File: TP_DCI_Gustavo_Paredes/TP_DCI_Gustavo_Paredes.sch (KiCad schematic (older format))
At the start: 6 parts, among them X701DB9F/90 DB9_Female, X702DB9M/90 DB9_Male

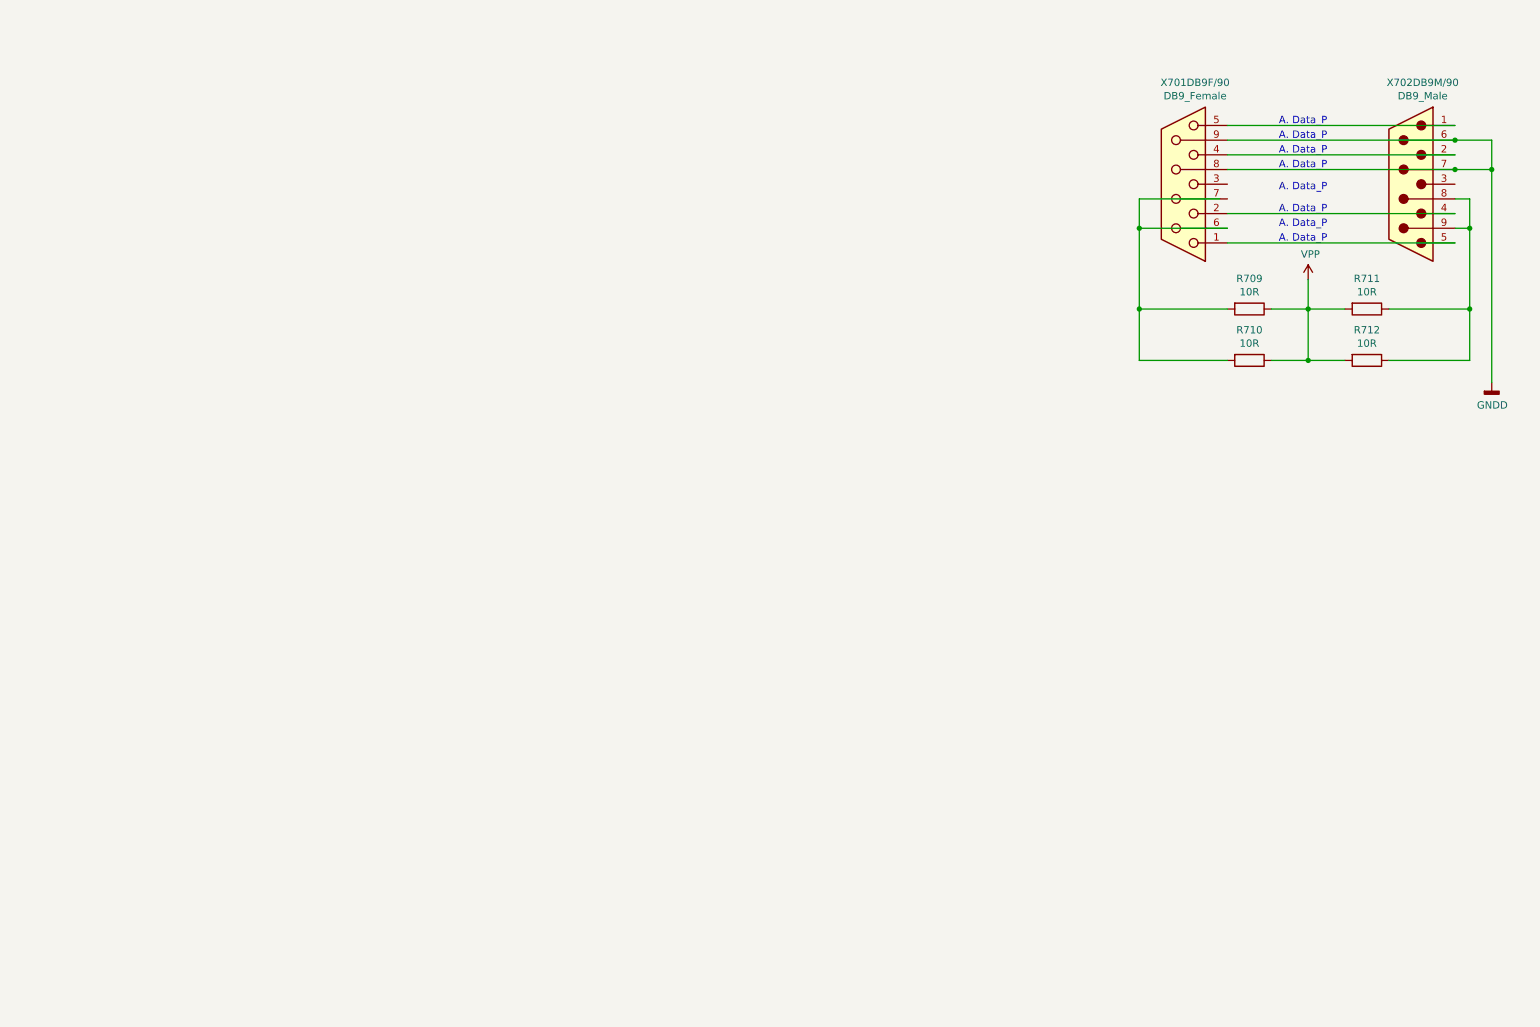
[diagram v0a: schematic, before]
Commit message: Conecciones externas DB9
Se conectaron las conexiones externas del DB9.
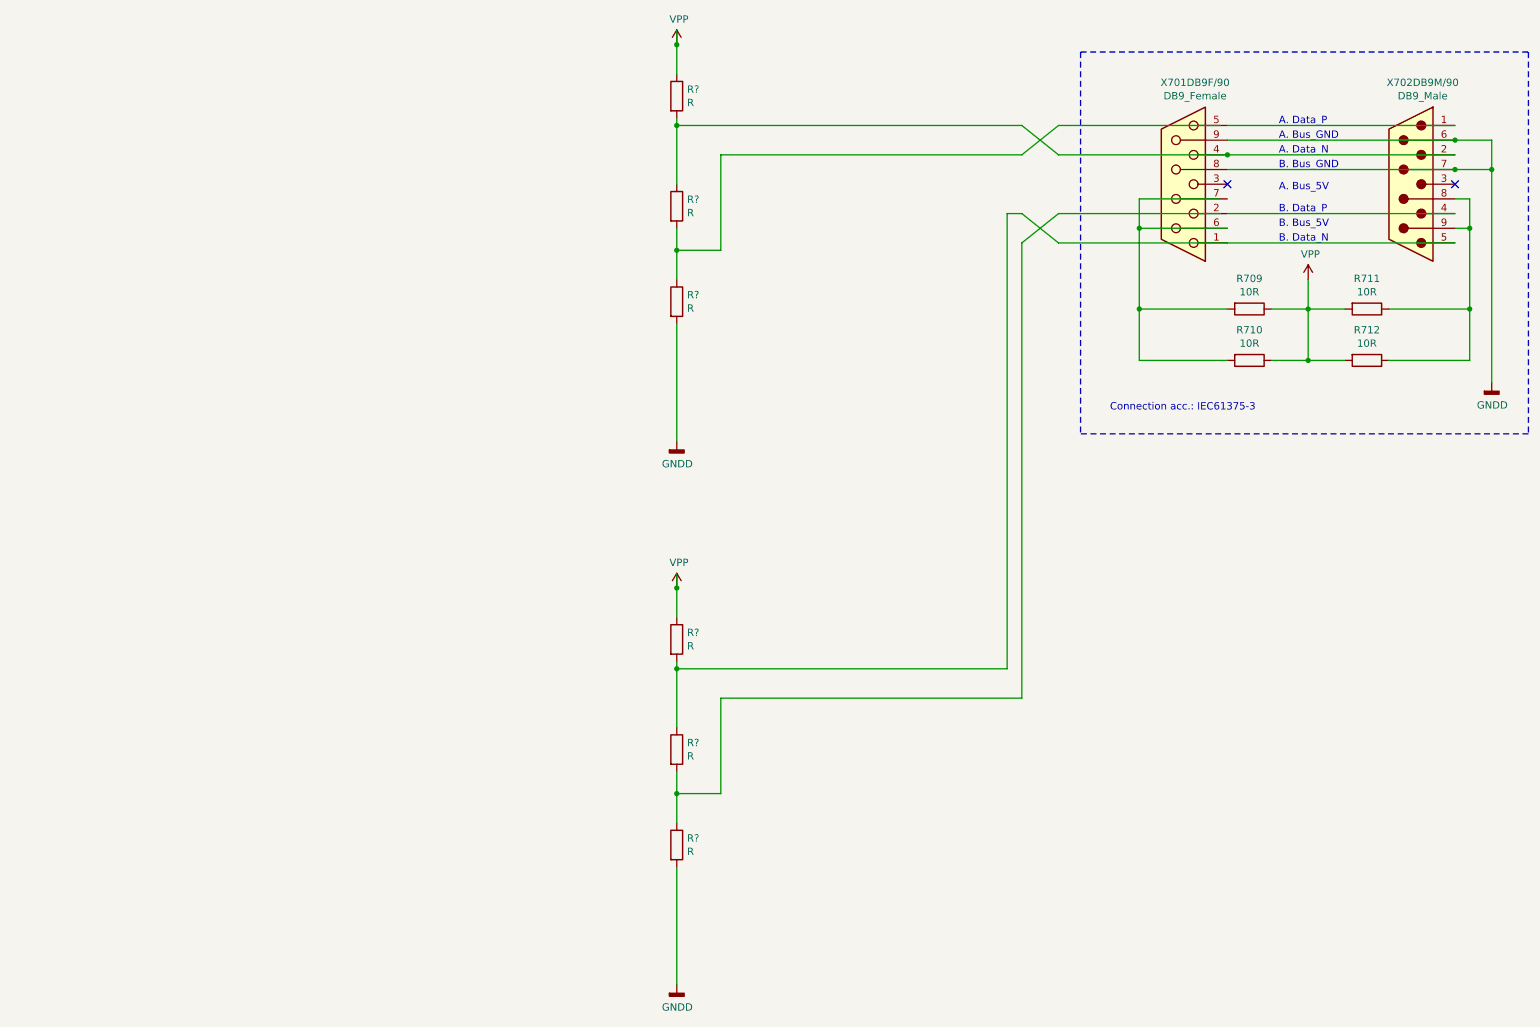
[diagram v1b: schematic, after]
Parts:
- added R? (x6): R, symbol Device:R
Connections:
- wire segments 30 -> 63
- no-connect marks 0 -> 2
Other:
- note added: "A. Bus_5V"
- note added: "A. Bus_GND"
- note added: "A. Data_N"
- note added: "B. Bus_5V"
- note added: "B. Bus_GND"
- note added: "B. Data_N"
- note added: "B. Data_P"
- note added: "Connection acc.: IEC61375-3"
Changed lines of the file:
@@
 A. Data_P
 Text Notes 9250 1500 0    50   ~ 0
-A. Data_P
+A. Bus_GND
 Text Notes 9250 1600 0    50   ~ 0
-A. Data_P
+A. Data_N
 Text Notes 9250 1700 0    50   ~ 0
-A. Data_P
+B. Bus_GND
 Text Notes 9250 1850 0    50   ~ 0
-A. Data_P
+A. Bus_5V
 Text Notes 9250 2000 0    50   ~ 0
-A. Data_P
+B. Data_P
 Text Notes 9250 2100 0    50   ~ 0
-A. Data_P
+B. Bus_5V
 Text Notes 9250 2200 0    50   ~ 0
-A. Data_P
+B. Data_N
+NoConn ~ 10450 1800
+NoConn ~ 8900 1800
+Wire Notes Line width 20 style solid
+	7900 900  10950 900
+Wire Notes Line width 20 style solid
+	10950 900  10950 3500
+Wire Notes Line width 20 style solid
+	10950 3500 7900 3500
+Text Notes 8100 3350 0    50   ~ 0
+Connection acc.: IEC61375-3
+$Comp
+L Device:R R?
+U 1 1 5CE42F3F
+P 5150 1200
+F 0 "R?" H 5220 1246 50  0000 L CNN
+F 1 "R" H 5220 1155 50  0000 L CNN
+F 2 "" V 5080 1200 50  0001 C CNN
+F 3 "~" H 5150 1200 50  0001 C CNN
+	1    5150 1200
+	1    0    0    -1
+$EndComp
+$Comp
+L Device:R R?
+U 1 1 5CE430BC
+P 5150 1950
+F 0 "R?" H 5220 1996 50  0000 L CNN
+F 1 "R" H 5220 1905 50  0000 L CNN
+F 2 "" V 5080 1950 50  0001 C CNN
+F 3 "~" H 5150 1950 50  0001 C CNN
+	1    5150 1950
+	1    0    0    -1
+$EndComp
+$Comp
+L Device:R R?
+U 1 1 5CE430FA
+P 5150 2600
+F 0 "R?" H 5220 2646 50  0000 L CNN
+F 1 "R" H 5220 2555 50  0000 L CNN
+F 2 "" V 5080 2600 50  0001 C CNN
+F 3 "~" H 5150 2600 50  0001 C CNN
+	1    5150 2600
+	1    0    0    -1
+$EndComp
+$Comp
+L power:GNDD #PWR?
+U 1 1 5CE43170
+P 5150 3550
+F 0 "#PWR?" H 5150 3300 50  0001 C CNN
+F 1 "GNDD" H 5154 3395 50  0000 C CNN
+F 2 "" H 5150 3550 50  0001 C CNN
+F 3 "" H 5150 3550 50  0001 C CNN
+	1    5150 3550
+	1    0    0    -1
+$EndComp
+$Comp
+L power:VPP #PWR?
+U 1 1 5CE4319F
+P 5150 850
+F 0 "#PWR?" H 5150 700 50  0001 C CNN
+F 1 "VPP" H 5165 1023 50  0000 C CNN
+F 2 "" H 5150 850 50  0001 C CNN
+F 3 "" H 5150 850 50  0001 C CNN
+	1    5150 850
+	1    0    0    -1
+$EndComp
+Wire Wire Line
+	5150 2100 5150 2250
+Wire Wire Line
+	5150 2750 5150 3550
+Wire Wire Line
+	5150 750  5150 850
+Wire Wire Line
+	8850 1400 7750 1400
+Wire Wire Line
+	8900 1600 7750 1600
+Connection ~ 8900 1600
+Wire Wire Line
+	5150 850  5150 1050
+Connection ~ 5150 850
+Wire Wire Line
+	5150 1800 5150 1400
+Wire Wire Line
+	7500 1400 5150 1400
+Connection ~ 5150 1400
+Wire Wire Line
+	5150 1400 5150 1350
+Wire Wire Line
+	7500 1600 5450 1600
+Wire Wire Line
+	5450 1600 5450 2250
+Wire Wire Line
+	5450 2250 5150 2250
+Connection ~ 5150 2250
+Wire Wire Line
+	5150 2250 5150 2450
+Wire Wire Line
+	7750 1600 7500 1400
+Wire Wire Line
+	7750 1400 7500 1600
+$Comp
+L Device:R R?
+U 1 1 5CE4D6F2
+P 5150 4900
+F 0 "R?" H 5220 4946 50  0000 L CNN
+F 1 "R" H 5220 4855 50  0000 L CNN
+F 2 "" V 5080 4900 50  0001 C CNN
+F 3 "~" H 5150 4900 50  0001 C CNN
+	1    5150 4900
+	1    0    0    -1
+$EndComp
+$Comp
+L Device:R R?
+U 1 1 5CE4D6F9
+P 5150 5650
+F 0 "R?" H 5220 5696 50  0000 L CNN
+F 1 "R" H 5220 5605 50  0000 L CNN
+F 2 "" V 5080 5650 50  0001 C CNN
+F 3 "~" H 5150 5650 50  0001 C CNN
+	1    5150 5650
+	1    0    0    -1
+$EndComp
+$Comp
+L Device:R R?
+U 1 1 5CE4D700
+P 5150 6300
+F 0 "R?" H 5220 6346 50  0000 L CNN
+F 1 "R" H 5220 6255 50  0000 L CNN
+F 2 "" V 5080 6300 50  0001 C CNN
+F 3 "~" H 5150 6300 50  0001 C CNN
+	1    5150 6300
+	1    0    0    -1
+$EndComp
+$Comp
+L power:GNDD #PWR?
+U 1 1 5CE4D707
+P 5150 7250
+F 0 "#PWR?" H 5150 7000 50  0001 C CNN
+F 1 "GNDD" H 5154 7095 50  0000 C CNN
+F 2 "" H 5150 7250 50  0001 C CNN
+F 3 "" H 5150 7250 50  0001 C CNN
+	1    5150 7250
+	1    0    0    -1
+$EndComp
+$Comp
+L power:VPP #PWR?
+U 1 1 5CE4D70D
+P 5150 4550
+F 0 "#PWR?" H 5150 4400 50  0001 C CNN
+F 1 "VPP" H 5165 4723 50  0000 C CNN
+F 2 "" H 5150 4550 50  0001 C CNN
+F 3 "" H 5150 4550 50  0001 C CNN
+	1    5150 4550
+	1    0    0    -1
+$EndComp
+Wire Wire Line
+	5150 5800 5150 5950
+Wire Wire Line
+	5150 6450 5150 7250
+Wire Wire Line
+	5150 4450 5150 4550
+Wire Wire Line
+	5150 4550 5150 4750
+Connection ~ 5150 4550
+Wire Wire Line
+	5450 5300 5450 5950
+Wire Wire Line
+	5450 5950 5150 5950
+Connection ~ 5150 5950
+Wire Wire Line
+	5150 5950 5150 6150
+Wire Wire Line
+	8850 2000 7750 2000
+Wire Wire Line
+	8900 2200 7750 2200
+Wire Wire Line
+	7750 2200 7500 2000
+Wire Wire Line
+	7750 2000 7500 2200
+Wire Wire Line
+	5150 5050 5150 5100
+Wire Wire Line
+	7500 2200 7500 5300
+Wire Wire Line
+	7500 5300 5450 5300
+Wire Wire Line
+	7500 2000 7400 2000
+Wire Wire Line
+	7400 2000 7400 5100
+Wire Wire Line
+	7400 5100 5150 5100
+Connection ~ 5150 5100
+Wire Wire Line
+	5150 5100 5150 5500
+Wire Notes Line width 20 style solid
+	7900 900  7900 3500
 $EndSCHEMATC

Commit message: Saco Ejercicios Practica Clases
Saco a un carpeta externa los ejercicios de las clases.
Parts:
- added C101, C102: 22nF, symbol Device:C
- added D101, D105: 4,7V, symbol Device:D_Zener
- added D102, D104, D106, D108: BAV99, symbol Diode:BAV99
- added D103, D107: 8,2V, symbol Device:D_Zener
- added R101, R102: 10K, symbol Device:R
- added U101, U102: LTC2861, Package_SO:SSOP-28_5.3x10.2mm_P0.65mm, symbol Interface_UART:LTC2861
- R103, R105, R106, R108: renamed from R?; value R -> 68K
- R104, R107: renamed from R?; value R -> 27K
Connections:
- net labels added: LINE_A_D0, LINE_A_D1, LINE_A_SF, LINE_B_D0, LINE_B_D1, LINE_B_SF, P701
- wire segments 63 -> 140
- no-connect marks 2 -> 6
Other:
- note added: "BZX84C4V7"
- note added: "BZX84C8V2"
- note added: "RS485: LINE_A_SF, LINE_A_D0, LINE_A_D1\n LINE_B_SF, LINE_B_D0, LINE_B_D1"
- moved on the sheet: R103, R104, R105, R106, R107, R108

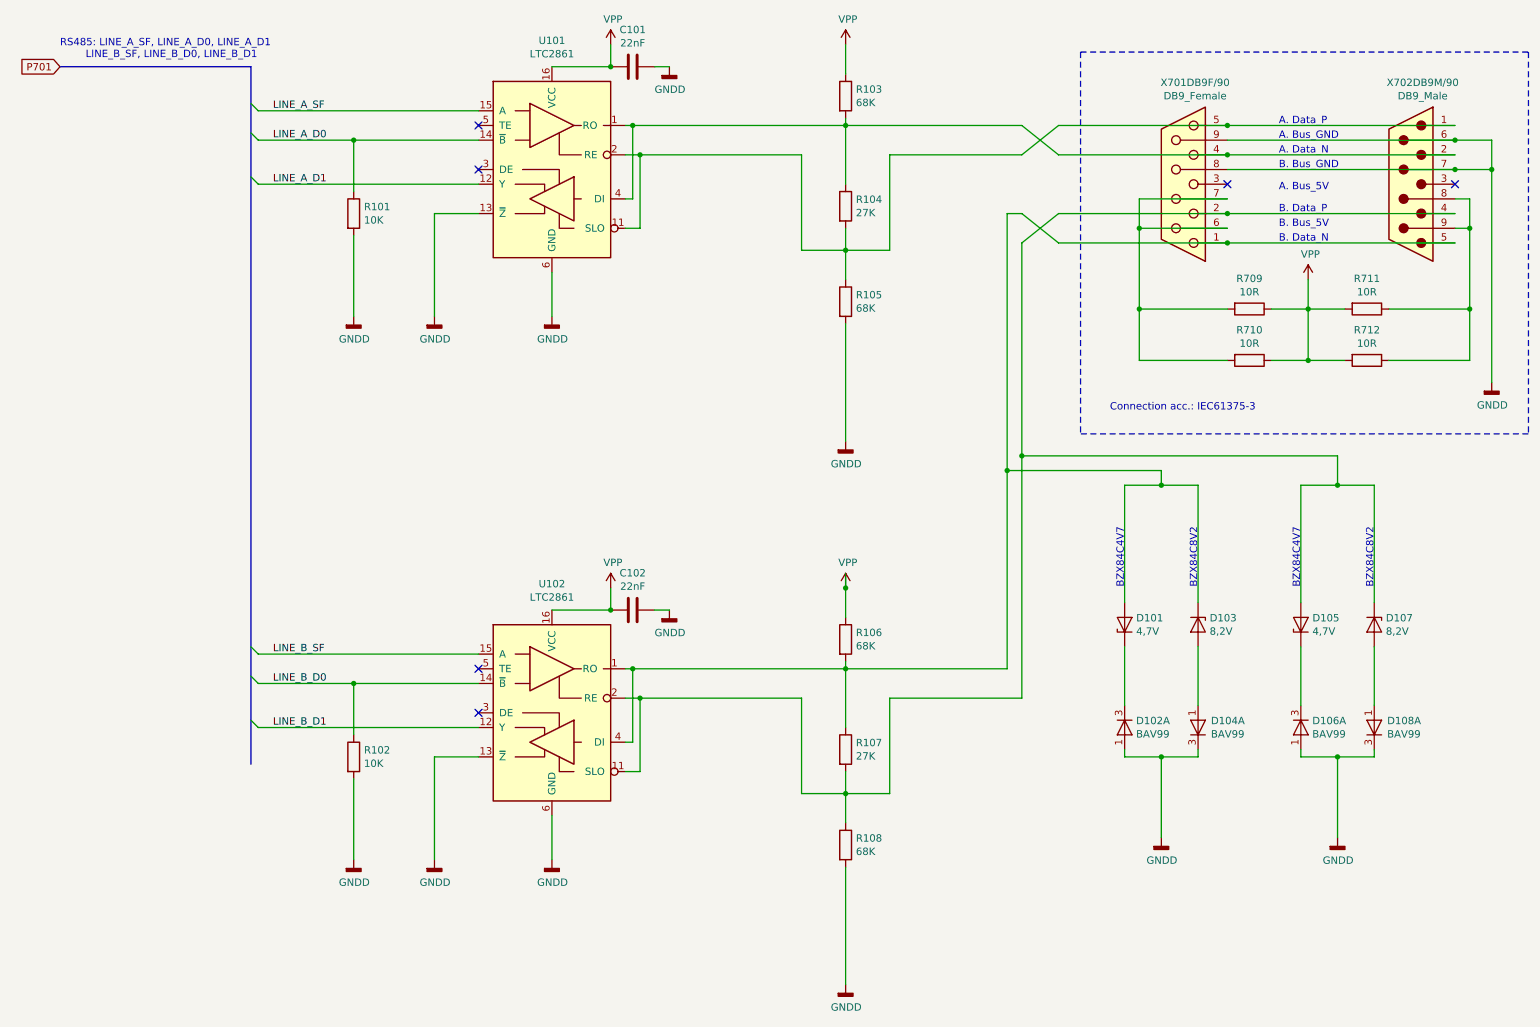
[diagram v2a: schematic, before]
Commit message: Arreglo algunos Errores electricos
Se repararon algunos errores del chequeo electrico, pero no todos.
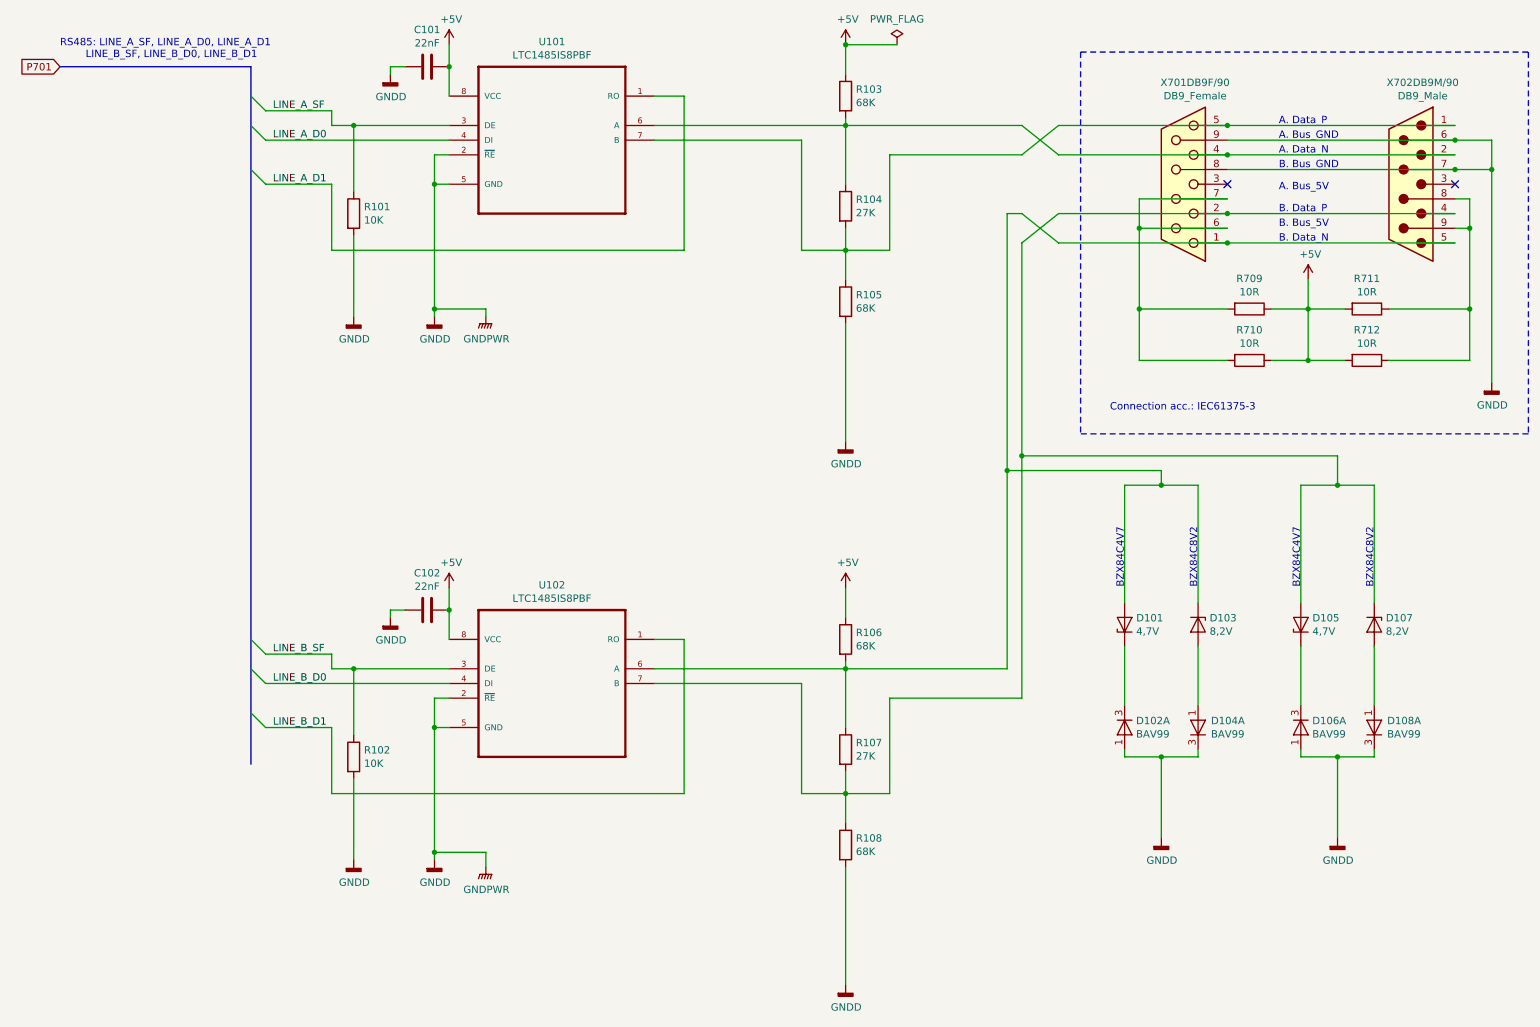
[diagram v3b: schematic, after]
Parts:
- removed U101, U102: LTC2861, Package_SO:SSOP-28_5.3x10.2mm_P0.65mm, symbol Interface_UART:LTC2861
- added U101, U102: LTC1485IS8PBF, SOIC127P600X175-8N, symbol LTC1485IS8PBF:LTC1485IS8PBF
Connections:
- net labels added: +5V, GNDPWR
- net labels removed: VPP
- wire segments 140 -> 144
- no-connect marks 6 -> 2
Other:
- moved on the sheet: C101

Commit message: Cambios Corrector
Realize los cambios propuestos por el compañero corrector.
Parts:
- removed D104: BAV99, symbol Diode:BAV99
- added unit 2 of D102
- added unit 1 of D105
- added D107, D110: 4,7V, symbol Device:D_Zener
- added unit 2 of D108
- added D109, D112: 8,2V, symbol Device:D_Zener
- added D111: BAV99, Package_TO_SOT_SMD:SOT-23, symbol Diode:BAV99
- D108: footprint (none) -> Package_TO_SOT_SMD:SOT-23
- renumbered D105 to D104, D106 to D105, D107 to D106, R709 to R109, R710 to R110, R711 to R111, R712 to R112, X701DB9F/90 to X701DB9F/101, X702DB9M/90 to X702DB9M/101
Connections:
- net GNDD: now also D102.3 (K), D105.3 (A), D108.1 (A), D102.3 (A), D105.3 (K), D108.2 (K), D111.1 (A), D111.2 (K); no longer D102.1 (A), D105.1 (A), D108.3 (K)
- net B_Data_N: now reaches R106.2, U102.6 (A), X701DB9F/101.1, X702DB9M/101.5
- net B_Data_N: now also D107.2 (A), D109.1 (K); no longer D101.2 (A), D103.1 (K), R107.1
- net A_Data_N: now reaches R103.2, R104.1, U101.6 (A), X701DB9F/101.4, X702DB9M/101.2
- net A_Data_N: now also D101.2 (A), D103.1 (K), R104.2, R105.1, U101.7 (B)
- net at D101.1 (K): now also D102.2 (K); no longer D102.3 (K)
- net at D103.2 (A): now also D102.1 (A)
- net at D104.1 (K): now also D105.2 (K); no longer D105.3 (K)
- net at D106.2 (A): now also D105.1 (A); no longer D108.1 (A)
- new net: R107.2, R108.1
- new net: D110.1 (K), D111.3 (K)
- new net: D111.3 (A), D112.2 (A)
- new net: D107.1 (K), D108.3 (K)
- new net: D108.3 (A), D109.2 (A)
- new net A_Data_P: D104.2 (A), D106.1 (K), X701DB9F/101.5, X702DB9M/101.1
- new net B_Data_P: D110.2 (A), D112.1 (K), U102.7 (B), X701DB9F/101.2, X702DB9M/101.4
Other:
- moved on the sheet: C102, D104, D106, R102, R104, R105, R106, R107, R108, U102
